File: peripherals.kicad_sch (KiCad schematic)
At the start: 26 parts, among them SW1 CHIP_EN, SW2 BTN1, SW3 BTN2, U4 AD623

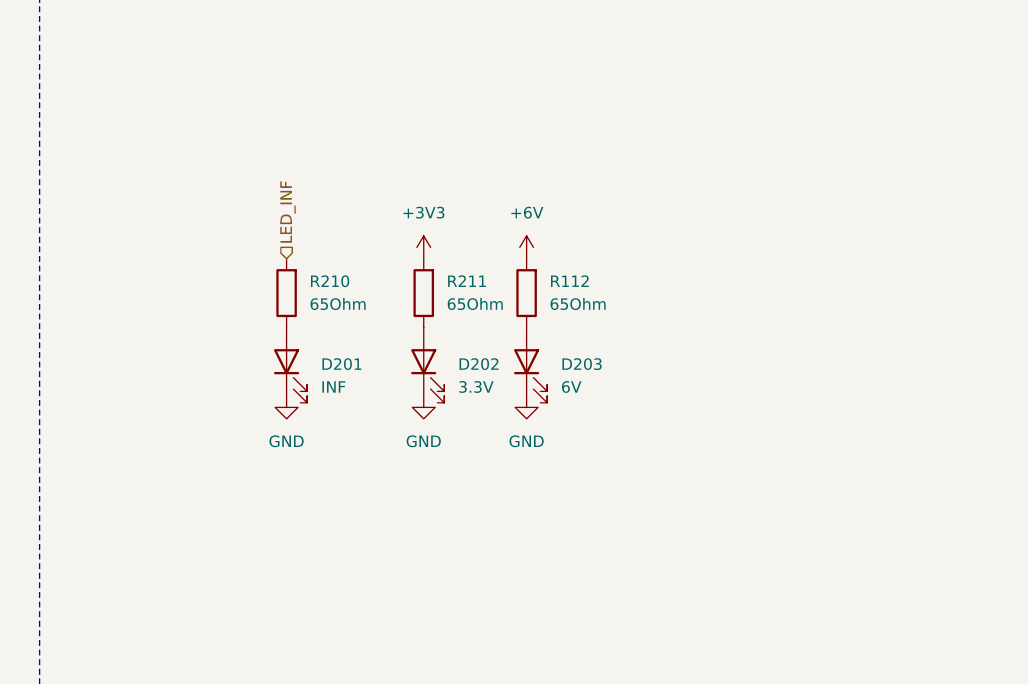
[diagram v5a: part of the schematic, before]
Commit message: feat: pcb almost done, added rgb led
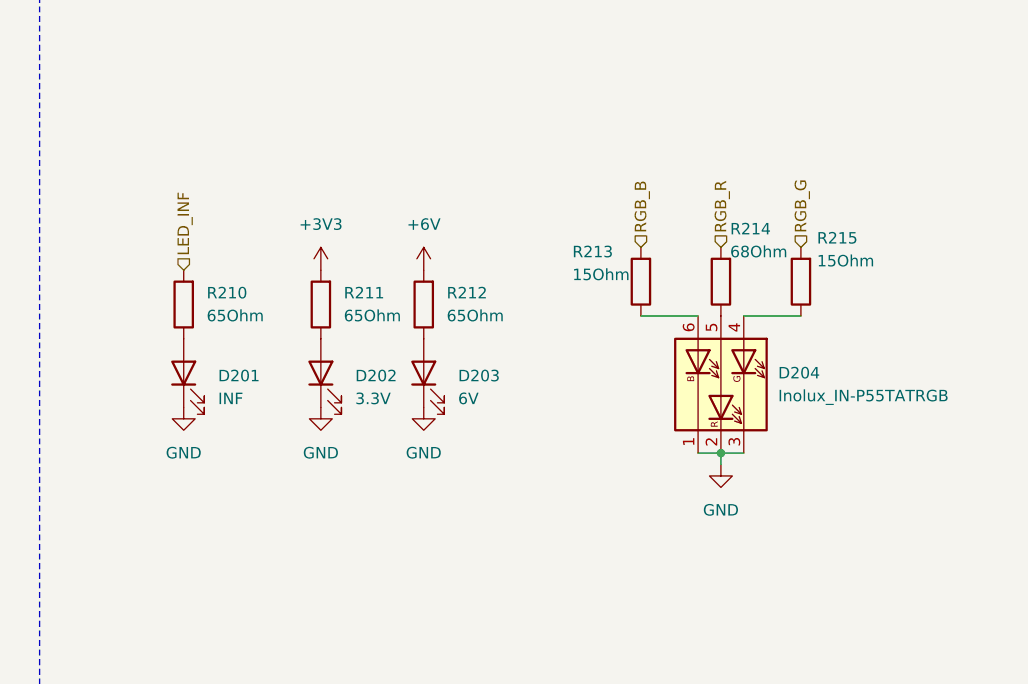
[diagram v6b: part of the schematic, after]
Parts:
- added D204: Inolux_IN-P55TATRGB, LED_SMD:LED_Inolux_IN-P55TATRGB_PLCC6_5.0x5.5mm_P1.8mm, symbol LED:Inolux_IN-P55TATRGB
- added R213, R215: 15Ohm, Resistor_SMD:R_0402_1005Metric_Pad0.72x0.64mm_HandSolder, symbol Device:R
- added R214: 68Ohm, Resistor_SMD:R_0402_1005Metric_Pad0.72x0.64mm_HandSolder, symbol Device:R
- renumbered R112 to R212
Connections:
- net GND: now also D204.1 (KB), D204.2 (KR), D204.3 (KG)
- new net: D204.4 (AG), R215.1
- new net: D204.5 (AR), R214.1
- new net: D204.6 (AB), R213.1
- new net RGB_B: R213.2
- new net RGB_G: R215.2
- new net RGB_R: R214.2
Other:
- moved on the sheet: D201, D202, D203, R210, R211, R212

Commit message: feat: silkscreen done
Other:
- company: (none) -> Mateusz Drogowski Karol Dworczyński
- title: (none) -> Drink Pouring Machine - Peripherals
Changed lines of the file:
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@@
 	(paper "A4")
 	(title_block
+		(title "Drink Pouring Machine - Peripherals")
 		(date "2025-12-08")
+		(rev "v1.0")
+		(company "Mateusz Drogowski Karol Dworczyński")
 	)
 	(text "Load Cell"

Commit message: fix: led resistor values, tensometer screw terminal
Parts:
- R210, R211: value 65Ohm -> 68Ohm
- R212: value 65Ohm -> 200Ohm
- SW1, SW2, SW3: footprint Button_Switch_SMD:SW_SPST_Omron_B3FS-100xP -> Button_Switch_SMD:SW_SPST_Omron_B3FS-101xP
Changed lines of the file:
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@@
 			)
 		)
-		(property "Value" "65Ohm"
+		(property "Value" "68Ohm"
 			(at 210.82 106.6799 0)
 			(effects
@@
 			)
 		)
-		(property "Value" "65Ohm"
+		(property "Value" "68Ohm"
 			(at 195.58 106.6799 0)
 			(effects
@@
 			)
 		)
-		(property "Footprint" "Button_Switch_SMD:SW_SPST_Omron_B3FS-100xP"
+		(property "Footprint" "Button_Switch_SMD:SW_SPST_Omron_B3FS-101xP"
 			(at 48.26 35.56 0)
 			(effects
@@
 			)
 		)
-		(property "Value" "65Ohm"
+		(property "Value" "200Ohm"
 			(at 222.25 106.6799 0)
 			(effects
@@
 			)
 		)
-		(property "Footprint" "Button_Switch_SMD:SW_SPST_Omron_B3FS-100xP"
+		(property "Footprint" "Button_Switch_SMD:SW_SPST_Omron_B3FS-101xP"
 			(at 95.25 34.29 0)
 			(effects
@@
 			)
 		)
-		(property "Footprint" "Button_Switch_SMD:SW_SPST_Omron_B3FS-100xP"
+		(property "Footprint" "Button_Switch_SMD:SW_SPST_Omron_B3FS-101xP"
 			(at 142.24 34.29 0)
 			(effects
